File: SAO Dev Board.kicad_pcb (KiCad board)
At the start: 2 copper layers, 140 x 140 mm, 59 parts, among them J1 4mm Banana, red, J2 4mm Banana, black, J3 Conn_02x03_Odd_Even, J4 Conn_02x02_Odd_Even, J5 Conn_02x02_Odd_Even, J6 LCSC C145956, J7 Conn_01x20_Socket, J8 Conn_01x20_Socket, SW1 5-Way_Switch, SW2 TS5220A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

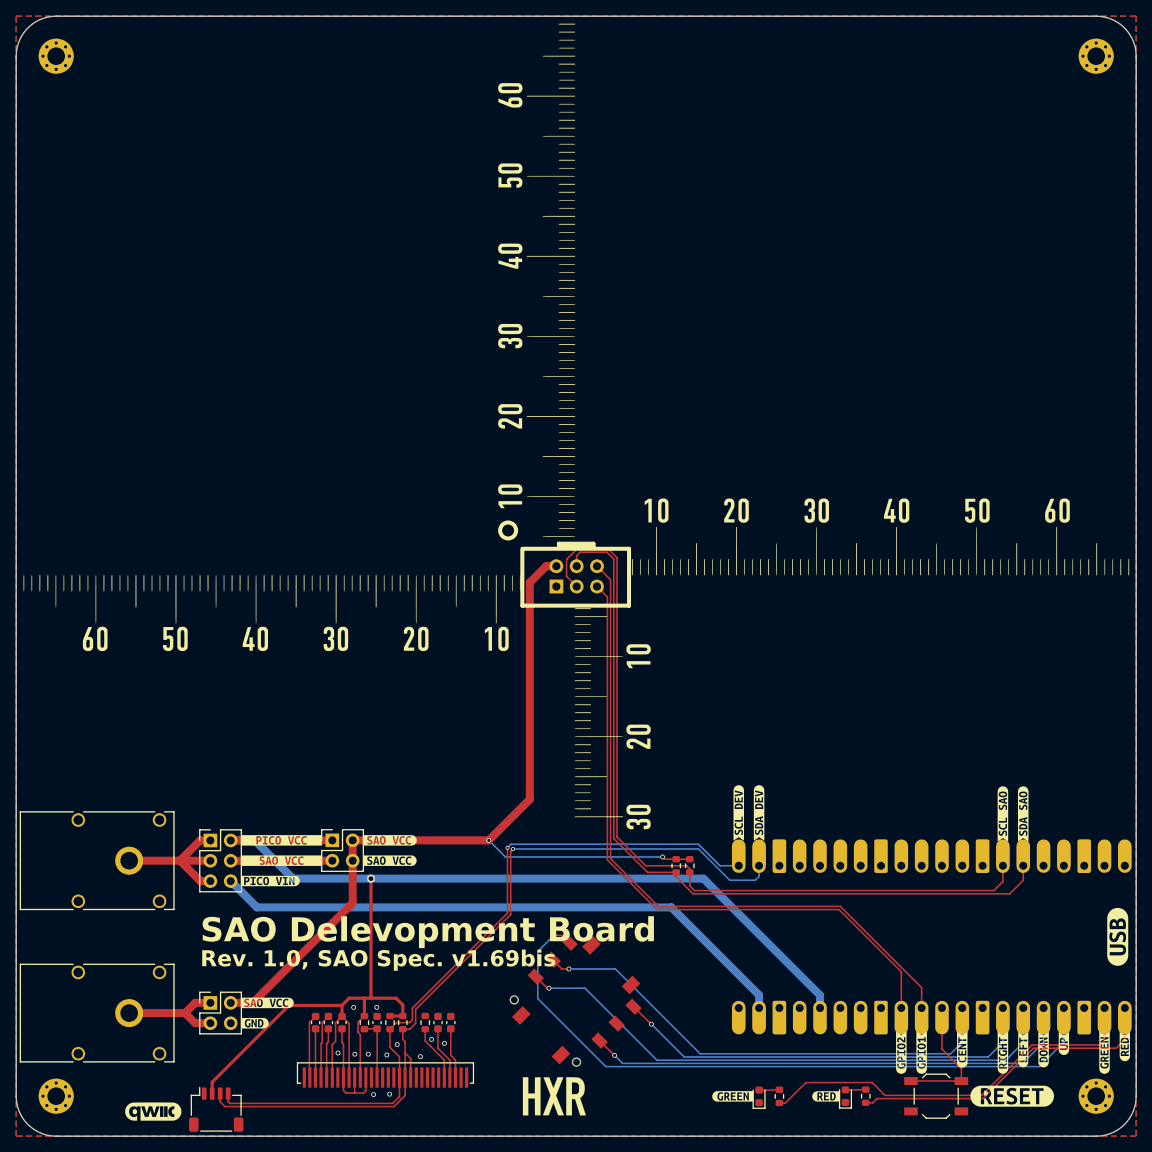
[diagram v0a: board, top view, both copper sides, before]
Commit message: Fixed rotated connector
Signed-off-by: Thomas Flummer <tf@flummer.net>
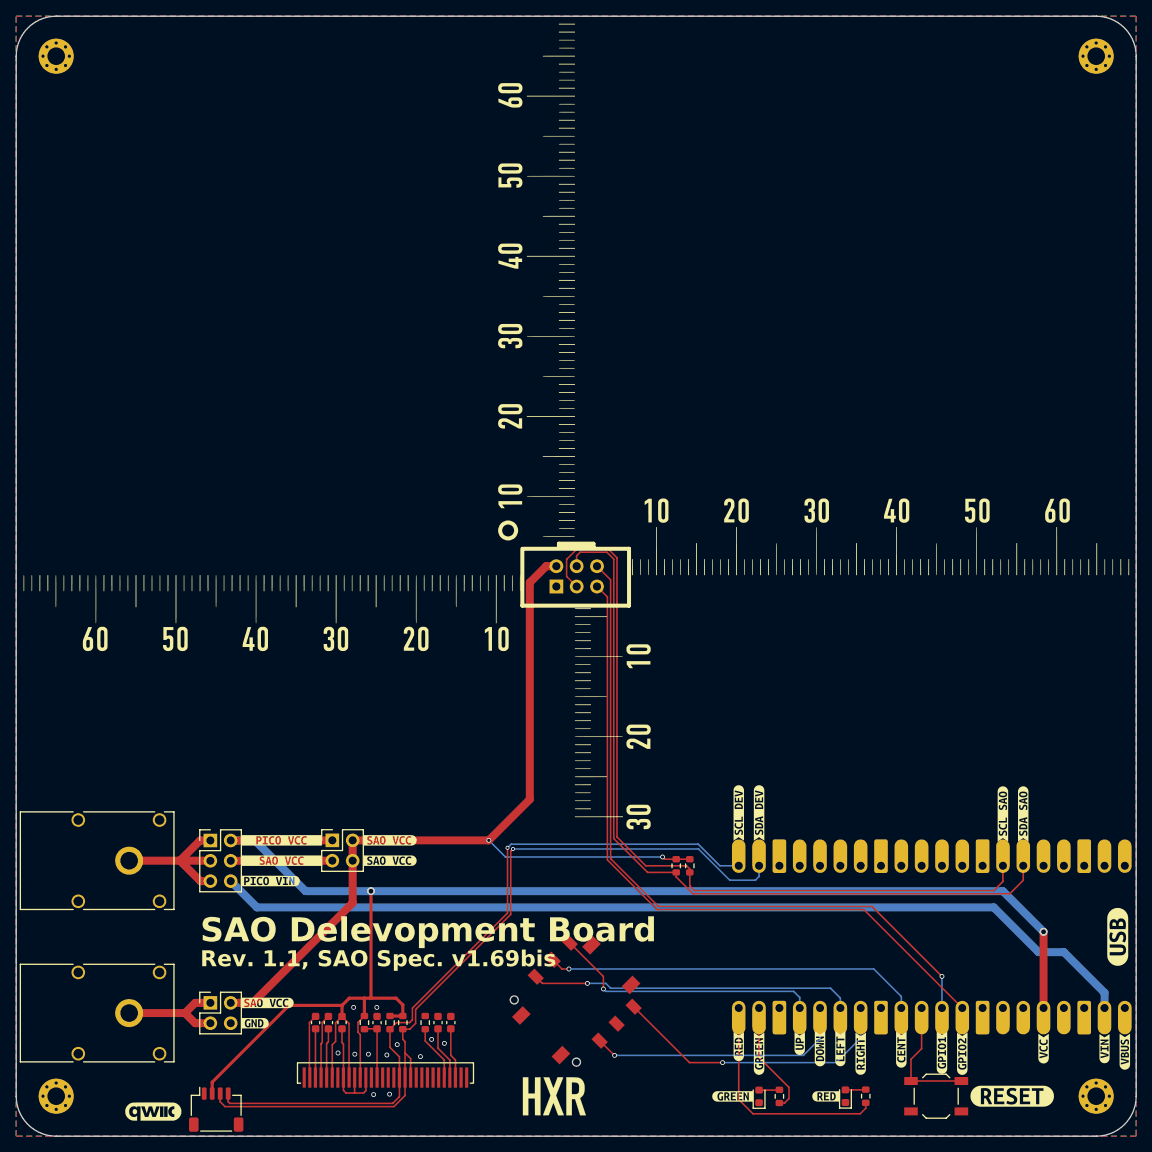
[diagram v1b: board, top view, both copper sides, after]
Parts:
- added kibuzzard-670E5162: G***, kibuzzard-670E5162, F.Cu at (158.4, 159.1)
- added kibuzzard-670E5178: G***, kibuzzard-670E5178, F.Cu at (168.6, 159.4)
- added kibuzzard-670E5189: G***, kibuzzard-670E5189, F.Cu at (166.0, 159.1)
- moved kibuzzard-66F97F8D 48.3 mm to (120.3, 158.8)
- moved J8 48.3 mm to (120.3, 154.0), turned to 90 degrees
- moved kibuzzard-66F97F94 43.2 mm to (122.9, 159.7)
- moved kibuzzard-66F97FA0 33.0 mm to (127.9, 158.4)
- moved kibuzzard-66F97FBA 27.9 mm to (130.5, 159.1)
- moved kibuzzard-66F97FD1 22.9 mm to (133.0, 159.1)
- moved kibuzzard-66F97FDE 17.8 mm to (135.6, 159.7)
- moved kibuzzard-66F97F40 7.62 mm to (148.3, 159.7)
- moved kibuzzard-66F98024 7.62 mm to (140.6, 159.2)
- moved kibuzzard-66F97F28 2.54 mm to (145.7, 159.6)
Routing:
- net BTN_UP: track 85.9 -> 33.8 mm
- net PICO_VIN: track 73.6 -> 116.9 mm
- net LED_GREEN: track 49.3 -> 14.3 mm
- net VCC: track 171.8 -> 202.8 mm, vias 1 -> 2
- net BTN_LEFT: track 70.5 -> 40.4 mm
- net BTN_DOWN: track 62.1 -> 33.0 mm
- net BTN_RIGHT: track 53.8 -> 36.3 mm
- net BTN_CENTER: track 60.9 -> 46.9 mm
- net LED_RED: track 39.6 -> 29.0 mm
- net SAO_GPIO2: track 81.8 -> 86.7 mm
- net SAO_GPIO1: track 85.4 -> 88.7 mm, vias 0 -> 1
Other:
- board text added: "Rev. 1.1, SAO Spec. v1.69bis"
- board text removed: "Rev. 1.0, SAO Spec. v1.69bis"
